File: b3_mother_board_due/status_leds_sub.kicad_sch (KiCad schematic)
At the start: 24 parts, among them Q10 BC547, Q5 BC547, Q6 BC547, Q7 BC547, Q8 BC547, Q9 BC547

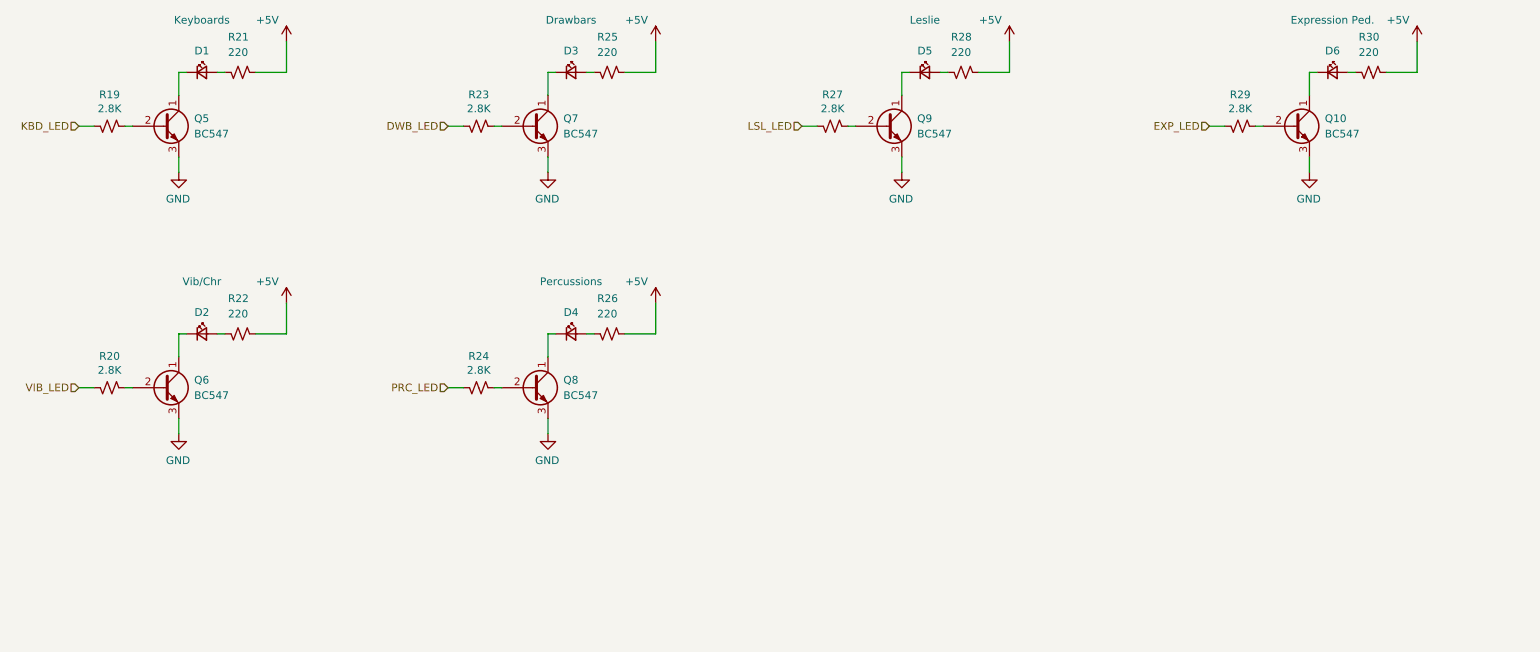
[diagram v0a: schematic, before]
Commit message: New organ architecture with mother board
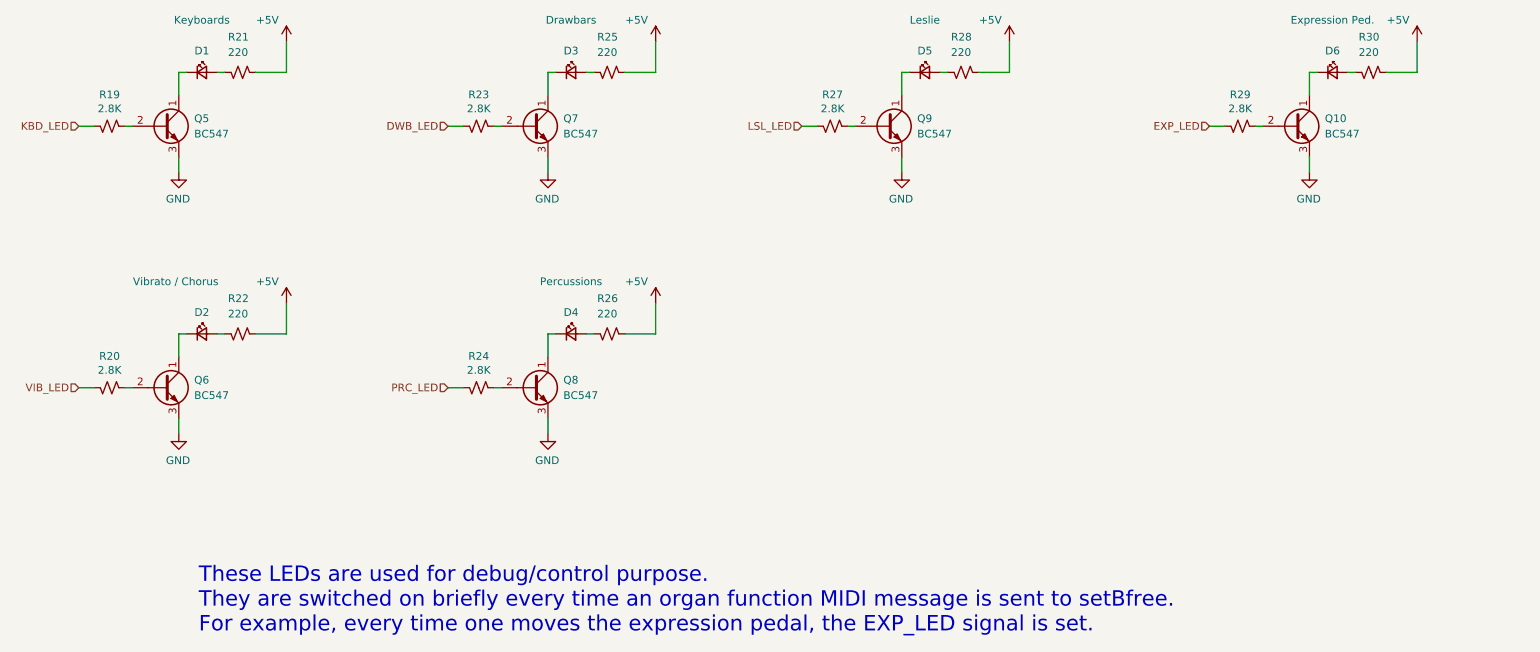
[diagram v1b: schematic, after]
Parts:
- D2: value Vib/Chr -> Vibrato / Chorus
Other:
- note added: "These LEDs are used for debug/control purpose. They are switched on briefly every time an organ function MIDI message is sent to setBfree. For example, every time one moves the expression pedal, the EXP_LED signal is set."
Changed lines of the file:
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@@
 	(title_block
 		(title "MIDI Message Sending Control LEDs")
-		(date "2024-11-16")
+		(date "2025-07-28")
 		(rev "1.0")
 		(company "Picherie")
+	)
+	(text "These LEDs are used for debug/control purpose.\nThey are switched on briefly every time an organ function MIDI message is sent to setBfree.\nFor example, every time one moves the expression pedal, the EXP_LED signal is set."
+		(exclude_from_sim no)
+		(at 56.642 129.032 0)
+		(effects
+			(font
+				(size 2.54 2.54)
+			)
+			(justify left)
+		)
 	)
 	(wire
@@
 			)
 		)
-		(property "Datasheet" "https://fr.farnell.com/on-semiconductor/bc547cbu/transistor-bipol-npn-45v-to-92/dp/2453791?st=bc547"
+		(property "Datasheet" "https://www.onsemi.com/pub/Collateral/BC550-D.pdf"
 			(at 50.8 50.8 0)
 			(effects
@@
 			)
 		)
-		(property "Description" ""
+		(property "Description" "0.1A Ic, 45V Vce, Small Signal NPN Transistor, TO-92"
 			(at 50.8 50.8 0)
 			(effects
@@
 			)
 		)
-		(property "Description" ""
+		(property "Description" "Power symbol creates a global label with name \"GND\" , ground"
 			(at 53.34 58.42 0)
 			(effects
@@
 			)
 		)
-		(property "Datasheet" "https://fr.farnell.com/panasonic/erj8enf2801v/res-couche-epaisse-2-8k-1-0-25w/dp/2307588"
+		(property "Datasheet" "~"
 			(at 102.87 93.98 0)
 			(effects
@@
 			)
 		)
-		(property "Description" ""
+		(property "Description" "Resistor, small US symbol"
 			(at 102.87 93.98 0)
 			(effects
@@
 			)
 		)
-		(property "Value" "Vib/Chr"
-			(at 57.15 76.454 0)
+		(property "Value" "Vibrato / Chorus"
+			(at 52.832 76.454 0)
 			(effects
 				(font
@@
 		)
 		(property "Description" "Light emitting diode, small symbol"
+			(at 57.15 85.09 0)
+			(effects
+				(font
+					(size 1.27 1.27)
+				)
+				(hide yes)
+			)
+		)
+		(property "Sim.Pin" "1=K 2=A"
 			(at 57.15 85.09 0)
 			(effects
@@
 			)
 		)
-		(property "Description" ""
+		(property "Description" "Power symbol creates a global label with name \"GND\" , ground"
 			(at 53.34 101.6 0)
 			(effects
@@
 			)
 		)
-		(property "Datasheet" "https://fr.farnell.com/panasonic/erj8enf2801v/res-couche-epaisse-2-8k-1-0-25w/dp/2307588"
+		(property "Datasheet" "~"
 			(at 161.29 50.8 0)
 			(effects
@@
 			)
 		)
-		(property "Description" ""
+		(property "Description" "Resistor, small US symbol"
 			(at 161.29 50.8 0)
 			(effects
@@
 			)
 		)
-		(property "Datasheet" "https://fr.farnell.com/on-semiconductor/bc547cbu/transistor-bipol-npn-45v-to-92/dp/2453791?st=bc547"
+		(property "Datasheet" "https://www.onsemi.com/pub/Collateral/BC550-D.pdf"
 			(at 170.18 50.8 0)
 			(effects
@@
 			)
 		)
-		(property "Description" ""
+		(property "Description" "0.1A Ic, 45V Vce, Small Signal NPN Transistor, TO-92"
 			(at 170.18 50.8 0)
 			(effects
@@
 			)
 		)
-		(property "Description" ""
+		(property "Description" "Power symbol creates a global label with name \"GND\" , ground"
 			(at 114.3 58.42 0)
 			(effects
@@
 			)
 		)
-		(property "Datasheet" "https://fr.farnell.com/panasonic/erj8enf2801v/res-couche-epaisse-2-8k-1-0-25w/dp/2307588"
+		(property "Datasheet" "~"
 			(at 41.91 93.98 0)
 			(effects
@@
 			)
 		)
-		(property "Description" ""
+		(property "Description" "Resistor, small US symbol"
 			(at 41.91 93.98 0)
 			(effects
@@
 			)
 		)
-		(property "Datasheet" "https://fr.farnell.com/on-semiconductor/bc547cbu/transistor-bipol-npn-45v-to-92/dp/2453791?st=bc547"
+		(property "Datasheet" "https://www.onsemi.com/pub/Collateral/BC550-D.pdf"
 			(at 111.76 93.98 0)
 			(effects
@@
 			)
 		)
-		(property "Description" ""
+		(property "Description" "0.1A Ic, 45V Vce, Small Signal NPN Transistor, TO-92"
 			(at 111.76 93.98 0)
 			(effects
@@
 			)
 		)
-		(property "Datasheet" "https://fr.farnell.com/on-semiconductor/bc547cbu/transistor-bipol-npn-45v-to-92/dp/2453791?st=bc547"
+		(property "Datasheet" "https://www.onsemi.com/pub/Collateral/BC550-D.pdf"
 			(at 111.76 50.8 0)
 			(effects
@@
 			)
 		)
-		(property "Description" ""
+		(property "Description" "0.1A Ic, 45V Vce, Small Signal NPN Transistor, TO-92"
 			(at 111.76 50.8 0)
 			(effects
@@
 			)
 		)
+		(property "Sim.Pin" "1=K 2=A"
+			(at 57.15 41.91 0)
+			(effects
+				(font
+					(size 1.27 1.27)
+				)
+				(hide yes)
+			)
+		)
 		(pin "1"
 		)
@@
 			)
 		)
-		(property "Datasheet" "https://fr.farnell.com/on-semiconductor/bc547cbu/transistor-bipol-npn-45v-to-92/dp/2453791?st=bc547"
+		(property "Datasheet" "https://www.onsemi.com/pub/Collateral/BC550-D.pdf"
 			(at 50.8 93.98 0)
 			(effects
@@
 			)
 		)
-		(property "Description" ""
+		(property "Description" "0.1A Ic, 45V Vce, Small Signal NPN Transistor, TO-92"
 			(at 50.8 93.98 0)
 			(effects
@@
 			)
 		)
-		(property "Description" ""
+		(property "Description" "Power symbol creates a global label with name \"GND\" , ground"
 			(at 172.72 58.42 0)
 			(effects
@@
 			)
 		)
-		(property "Description" ""
+		(property "Description" "Power symbol creates a global label with name \"GND\" , ground"
 			(at 114.3 101.6 0)
 			(effects
@@
 		)
 		(property "Description" "Light emitting diode, small symbol"
+			(at 176.53 41.91 0)
+			(effects
+				(font
+					(size 1.27 1.27)
+				)
+				(hide yes)
+			)
+		)
+		(property "Sim.Pin" "1=K 2=A"
 			(at 176.53 41.91 0)
 			(effects
@@
 			)
 		)
-		(property "Datasheet" "https://fr.farnell.com/panasonic/erj8enf2801v/res-couche-epaisse-2-8k-1-0-25w/dp/2307588"
+		(property "Datasheet" "~"
 			(at 228.6 50.8 0)
 			(effects
@@
 			)
 		)
-		(property "Description" ""
+		(property "Description" "Resistor, small US symbol"
 			(at 228.6 50.8 0)
 			(effects
@@
 			)
 		)
-		(property "Datasheet" "https://fr.farnell.com/panasonic/erj8enf2801v/res-couche-epaisse-2-8k-1-0-25w/dp/2307588"
+		(property "Datasheet" "~"
 			(at 102.87 50.8 0)
 			(effects
@@
 			)
 		)
-		(property "Description" ""
+		(property "Description" "Resistor, small US symbol"
 			(at 102.87 50.8 0)
 			(effects
@@
 		)
 		(property "Description" "Light emitting diode, small symbol"
+			(at 118.11 85.09 0)
+			(effects
+				(font
+					(size 1.27 1.27)
+				)
+				(hide yes)
+			)
+		)
+		(property "Sim.Pin" "1=K 2=A"
 			(at 118.11 85.09 0)
 			(effects
@@
 			)
 		)
-		(property "Datasheet" "https://fr.farnell.com/on-semiconductor/bc547cbu/transistor-bipol-npn-45v-to-92/dp/2453791?st=bc547"
+		(property "Datasheet" "https://www.onsemi.com/pub/Collateral/BC550-D.pdf"
 			(at 237.49 50.8 0)
 			(effects
@@
 			)
 		)
-		(property "Description" ""
+		(property "Description" "0.1A Ic, 45V Vce, Small Signal NPN Transistor, TO-92"
 			(at 237.49 50.8 0)
 			(effects
@@
 		)
 		(property "Description" "Light emitting diode, small symbol"
+			(at 118.11 41.91 0)
+			(effects
+				(font
+					(size 1.27 1.27)
+				)
+				(hide yes)
+			)
+		)
+		(property "Sim.Pin" "1=K 2=A"
 			(at 118.11 41.91 0)
 			(effects
@@
 			)
 		)
-		(property "Datasheet" "https://fr.farnell.com/panasonic/erj8enf2801v/res-couche-epaisse-2-8k-1-0-25w/dp/2307588"
+		(property "Datasheet" "~"
 			(at 41.91 50.8 0)
 			(effects
@@
 			)
 		)
-		(property "Description" ""
+		(property "Description" "Resistor, small US symbol"
 			(at 41.91 50.8 0)
 			(effects
@@
 		)
 		(property "Description" "Light emitting diode, small symbol"
+			(at 243.84 41.91 0)
+			(effects
+				(font
+					(size 1.27 1.27)
+				)
+				(hide yes)
+			)
+		)
+		(property "Sim.Pin" "1=K 2=A"
 			(at 243.84 41.91 0)
 			(effects
@@
 			)
 		)
-		(property "Description" ""
+		(property "Description" "Power symbol creates a global label with name \"GND\" , ground"
 			(at 240.03 58.42 0)
 			(effects
